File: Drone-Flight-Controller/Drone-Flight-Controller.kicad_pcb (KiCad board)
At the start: 2 copper layers, 30 x 65 mm, 60 parts, among them J1 TestPoint, J10 TestPoint, J11 TestPoint, J12 TestPoint, J13 TestPoint, J2 TestPoint, J3 2044-2X20G00RA, J4 TestPoint, J5 TestPoint, J6 TestPoint, J7 TestPoint, J8 TestPoint, J9 TestPoint, Q2 BSS138, Q3 BSS138, Q4 BSS138, Q5 BSS138, SW1 TL3301NF160QG-KR, U1 MCP1700T-1802E/MB, U2 LMR51430, U3 ADC101C021CIMK, U4 ICM-20948, U6 PCA9531PW, U7 BMP390

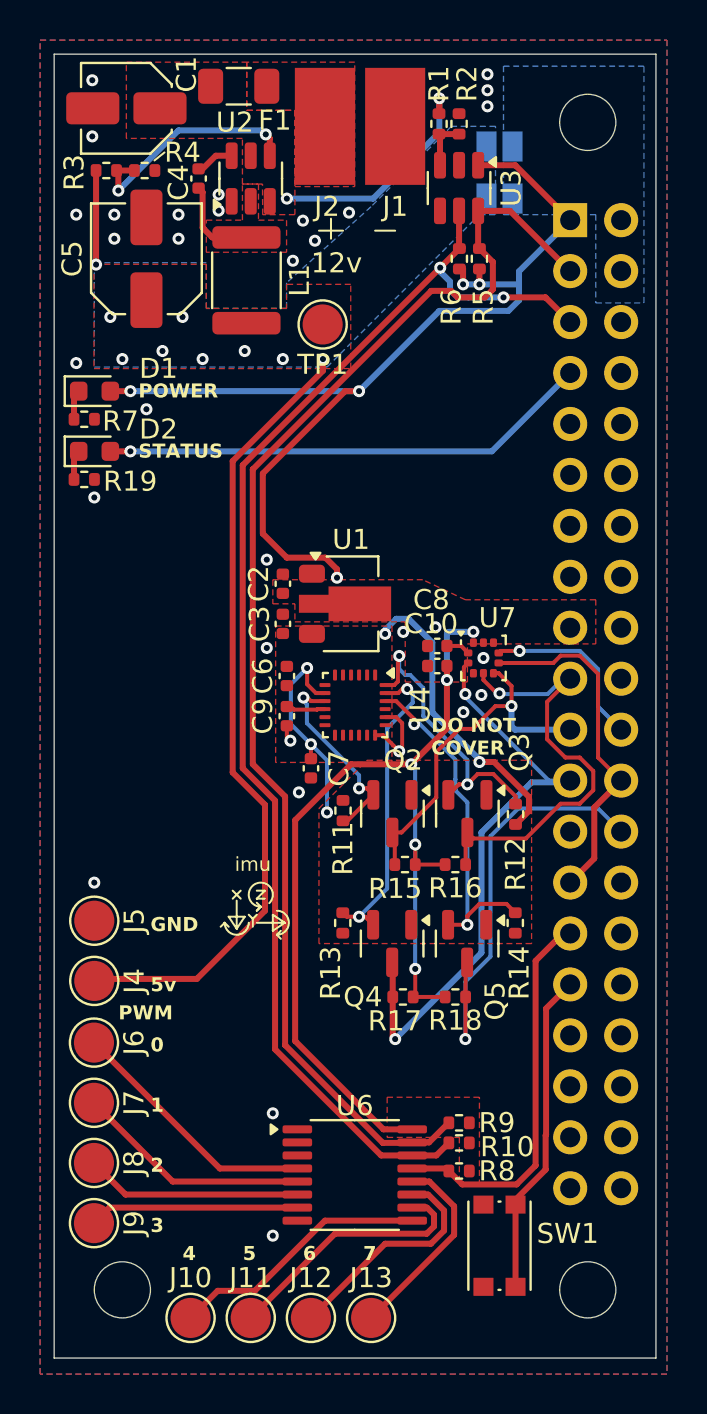
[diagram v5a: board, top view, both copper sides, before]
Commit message: i2c to pwm is now a pca9685
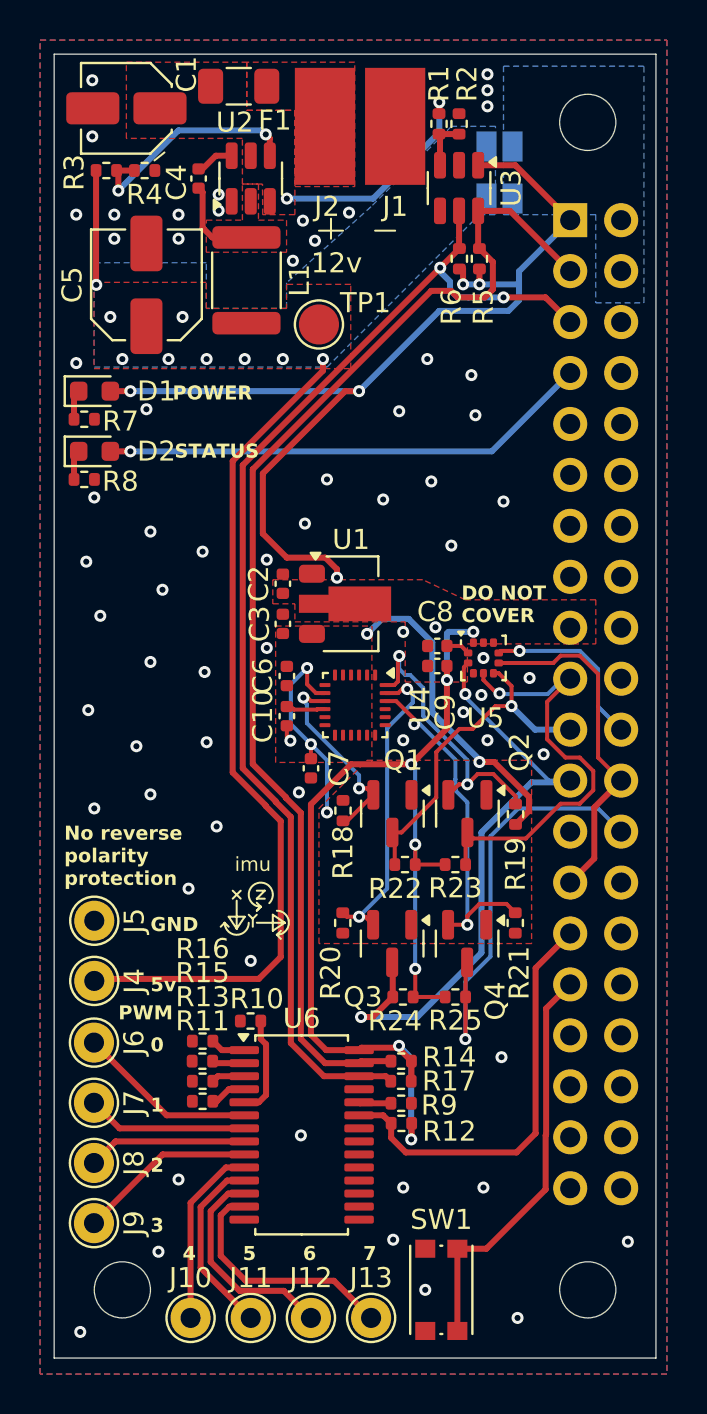
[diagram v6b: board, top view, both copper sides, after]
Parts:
- added R10: RK73G1ERTTP1002F, Resistor_SMD:R_0402_1005Metric, F.Cu at (22.0, 60.4)
- added R11: RK73G1ERTTP1002F, Resistor_SMD:R_0402_1005Metric, F.Cu at (19.6, 64.4)
- added R13: RK73G1ERTTP1002F, Resistor_SMD:R_0402_1005Metric, F.Cu at (19.6, 63.4)
- added R15: RK73G1ERTTP1002F, Resistor_SMD:R_0402_1005Metric, F.Cu at (19.6, 62.4)
- added R16: RK73G1ERTTP1002F, Resistor_SMD:R_0402_1005Metric, F.Cu at (19.6, 61.4)
- added R9: RK73G1ERTTP1002F, Resistor_SMD:R_0402_1005Metric, F.Cu at (29.5, 64.5)
- U6: value PCA9531PW -> PCA9685PW; footprint Package_SO:TSSOP-16_4.4x5mm_P0.65mm -> Package_SO:TSSOP-28_4.4x9.7mm_P0.65mm
- moved R17 4.22 mm to (29.5, 63.4)
- moved R14 4.22 mm to (29.5, 62.4)
- moved R12 3.73 mm to (29.5, 65.5)
- moved SW1 3.64 mm to (31.5, 73.8)
- moved U6 3.32 mm to (24.5, 66.1)
- moved C5 1.30 mm to (16.8, 23.7)
- moved TP1 0.19 mm to (25.4, 25.7)
- renumbered C9 to C10, C10 to C9, Q2 to Q1, Q3 to Q2, Q4 to Q3, Q5 to Q4, R8 to R12, R9 to R14, R10 to R17, R11 to R18, R12 to R19, R13 to R20, R14 to R21, R15 to R22, R16 to R23, R17 to R24, R18 to R25, R19 to R8, U7 to U5
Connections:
- U6 pad 1: GND -> Net-(U6-A0)
- U6 pad 10: PWM_5 -> PWM_4
- U6 pad 11: PWM_6 -> PWM_5
- U6 pad 12: PWM_7 -> PWM_6
- U6 pad 13: PWM_RESET -> PWM_7
- U6 pad 14: I2C_SCL -> GND
- U6 pad 15: I2C_SDA -> unconnected-(U6-LED8-Pad15)
- U6 pad 16: +3.3V -> unconnected-(U6-LED9-Pad16)
- U6 pad 2: GND -> Net-(U6-A1)
- U6 pad 3: GND -> Net-(U6-A2)
- U6 pad 4: PWM_0 -> Net-(U6-A3)
- U6 pad 5: PWM_1 -> Net-(U6-A4)
- U6 pad 6: PWM_2 -> PWM_0
- U6 pad 7: PWM_3 -> PWM_1
- U6 pad 8: GND -> PWM_2
- U6 pad 9: PWM_4 -> PWM_3
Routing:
- net I2C_SDA: track 66.0 -> 60.4 mm
- net I2C_SCL: track 66.2 -> 60.9 mm
- net Net-(U6-A4): track 0.00 -> 5.04 mm
- net Net-(J3-GPCLK2/GPIO06): track 16.2 -> 20.5 mm
- net +3.3V: track 102.6 -> 106.7 mm, vias 10 -> 12
- net GND: track 4.58 -> 0.62 mm, vias 32 -> 68
- net PWM_4: track 13.1 -> 9.14 mm
- net PWM_1: track 11.8 -> 8.02 mm
- net PWM_0: track 12.7 -> 8.99 mm
- net PWM_5: track 12.8 -> 9.29 mm
- net +5V: track 44.5 -> 48.0 mm
- net PWM_2: track 10.8 -> 7.94 mm
- net PWM_7: track 9.88 -> 12.2 mm
- net Net-(U6-A3): track 0.00 -> 1.81 mm
- net Net-(U6-A0): track 0.00 -> 1.75 mm
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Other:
- board text added: "No reverse polarity protection"
